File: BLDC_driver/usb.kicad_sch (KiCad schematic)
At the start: 4 parts, among them J5 USB-C 16P, U6 USBLC6-2SC6

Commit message: Update
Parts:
- FL1: footprint Marijn_KiCad:ACM2012_TDK_UPDATE -> Marijn_KiCad:ACM2012_900_2P_T002_Correct
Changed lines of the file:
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@@
 			)
 		)
-		(property "Footprint" "Marijn_KiCad:ACM2012_TDK_UPDATE"
+		(property "Footprint" "Marijn_KiCad:ACM2012_900_2P_T002_Correct"
 			(at 80.01 45.72 0)
 			(effects
@@
 			(project "Keyboard_PCB"
 				(path "/55e5f9ee-4ad9-4c00-8411-66894e392a47/980bf964-91c2-4997-a9de-db50a0c197aa"
+					(reference "FL1")
+					(unit 1)
+				)
+			)
+			(project ""
+				(path "/6f399879-dc45-4210-87b6-ea005f89c132/bcef801b-ac65-4b5b-aaac-ab2b26da4b0f"
 					(reference "FL1")
 					(unit 1)
@@
 				)
 			)
+			(project ""
+				(path "/6f399879-dc45-4210-87b6-ea005f89c132/bcef801b-ac65-4b5b-aaac-ab2b26da4b0f"
+					(reference "R6")
+					(unit 1)
+				)
+			)
 			(project "Keyboard_PCB"
 				(path "/dd51e792-c76c-4d43-96de-494177f3b593/f183b390-0c59-4c65-8a55-408064b389c7"
@@
 				)
 			)
+			(project ""
+				(path "/6f399879-dc45-4210-87b6-ea005f89c132/bcef801b-ac65-4b5b-aaac-ab2b26da4b0f"
+					(reference "#PWR024")
+					(unit 1)
+				)
+			)
 			(project "Keyboard_PCB"
 				(path "/dd51e792-c76c-4d43-96de-494177f3b593/f183b390-0c59-4c65-8a55-408064b389c7"
@@
 				)
 			)
+			(project ""
+				(path "/6f399879-dc45-4210-87b6-ea005f89c132/bcef801b-ac65-4b5b-aaac-ab2b26da4b0f"
+					(reference "U3")
+					(unit 1)
+				)
+			)
 			(project "Keyboard_PCB"
 				(path "/dd51e792-c76c-4d43-96de-494177f3b593/f183b390-0c59-4c65-8a55-408064b389c7"
@@
 				)
 			)
+			(project ""
+				(path "/6f399879-dc45-4210-87b6-ea005f89c132/bcef801b-ac65-4b5b-aaac-ab2b26da4b0f"
+					(reference "#PWR027")
+					(unit 1)
+				)
+			)
 			(project "Keyboard_PCB"
 				(path "/dd51e792-c76c-4d43-96de-494177f3b593/f183b390-0c59-4c65-8a55-408064b389c7"
@@
 				)
 			)
+			(project ""
+				(path "/6f399879-dc45-4210-87b6-ea005f89c132/bcef801b-ac65-4b5b-aaac-ab2b26da4b0f"
+					(reference "J4")
+					(unit 1)
+				)
+			)
 			(project "Keyboard_PCB"
 				(path "/dd51e792-c76c-4d43-96de-494177f3b593/f183b390-0c59-4c65-8a55-408064b389c7"
@@
 				)
 			)
+			(project ""
+				(path "/6f399879-dc45-4210-87b6-ea005f89c132/bcef801b-ac65-4b5b-aaac-ab2b26da4b0f"
+					(reference "#PWR025")
+					(unit 1)
+				)
+			)
 			(project "Keyboard_PCB"
 				(path "/dd51e792-c76c-4d43-96de-494177f3b593/f183b390-0c59-4c65-8a55-408064b389c7"
@@
 				)
 			)
+			(project ""
+				(path "/6f399879-dc45-4210-87b6-ea005f89c132/bcef801b-ac65-4b5b-aaac-ab2b26da4b0f"
+					(reference "#PWR026")
+					(unit 1)
+				)
+			)
 			(project "Keyboard_PCB"
 				(path "/dd51e792-c76c-4d43-96de-494177f3b593/f183b390-0c59-4c65-8a55-408064b389c7"
@@
 					(unit 1)
 				)
+			)
+			(project ""
+				(path "/6f399879-dc45-4210-87b6-ea005f89c132/bcef801b-ac65-4b5b-aaac-ab2b26da4b0f"
+					(reference "#PWR023")
+					(unit 1)
+				)

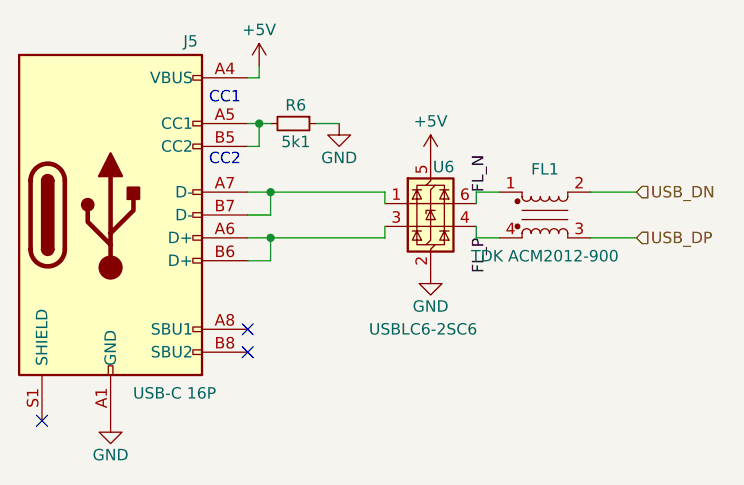
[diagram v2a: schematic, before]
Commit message: Started on power conversion section
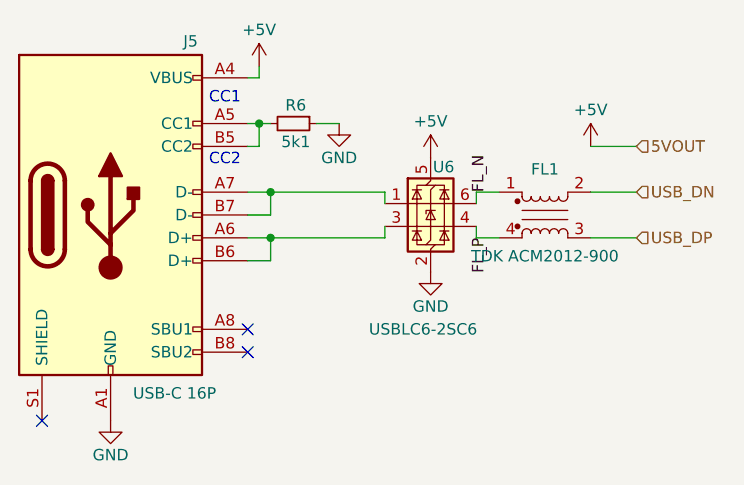
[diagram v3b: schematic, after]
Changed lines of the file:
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@@
+	(wire
+		(pts
+			(xy 90.17 31.75) (xy 85.09 31.75)
+		)
+		(stroke
+			(width 0)
+			(type default)
+		)
+	)
 	(wire
 		(pts
@@
 			)
 			(justify left bottom)
+		)
+	)
+	(hierarchical_label "5VOUT"
+		(shape input)
+		(at 90.17 31.75 0)
+		(fields_autoplaced yes)
+		(effects
+			(font
+				(size 1.27 1.27)
+			)
+			(justify left)
 		)
 	)
@@
 					(unit 1)
 				)
+			)
+		)
+	)
+	(symbol
+		(lib_id "power:+5V")
+		(at 85.09 31.75 0)
+		(unit 1)
+		(exclude_from_sim no)
+		(in_bom yes)
+		(on_board yes)
+		(dnp no)
+		(property "Reference" "#PWR057"
+			(at 85.09 35.56 0)
+			(effects
+				(font
+					(size 1.27 1.27)
+				)
+				(hide yes)
+			)
+		)
+		(property "Value" "+5V"
+			(at 85.09 27.686 0)
+			(effects
+				(font
+					(size 1.27 1.27)
+				)
+			)
+		)
+		(property "Footprint" ""
+			(at 85.09 31.75 0)
+			(effects
+				(font
+					(size 1.27 1.27)
+				)
+				(hide yes)
+			)
+		)
+		(property "Datasheet" ""
+			(at 85.09 31.75 0)
+			(effects
+				(font
+					(size 1.27 1.27)
+				)
+				(hide yes)
+			)
+		)
+		(property "Description" "Power symbol creates a global label with name \"+5V\""
+			(at 85.09 31.75 0)
+			(effects
+				(font
+					(size 1.27 1.27)
+				)
+				(hide yes)
+			)
+		)
+		(pin "1"
+		)
+		(instances
+			(project "BLDC_driver"
+				(path "/6f399879-dc45-4210-87b6-ea005f89c132/bcef801b-ac65-4b5b-aaac-ab2b26da4b0f"
+					(reference "#PWR057")
+					(unit 1)
+				)
